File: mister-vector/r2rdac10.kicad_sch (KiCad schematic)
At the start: 20 parts

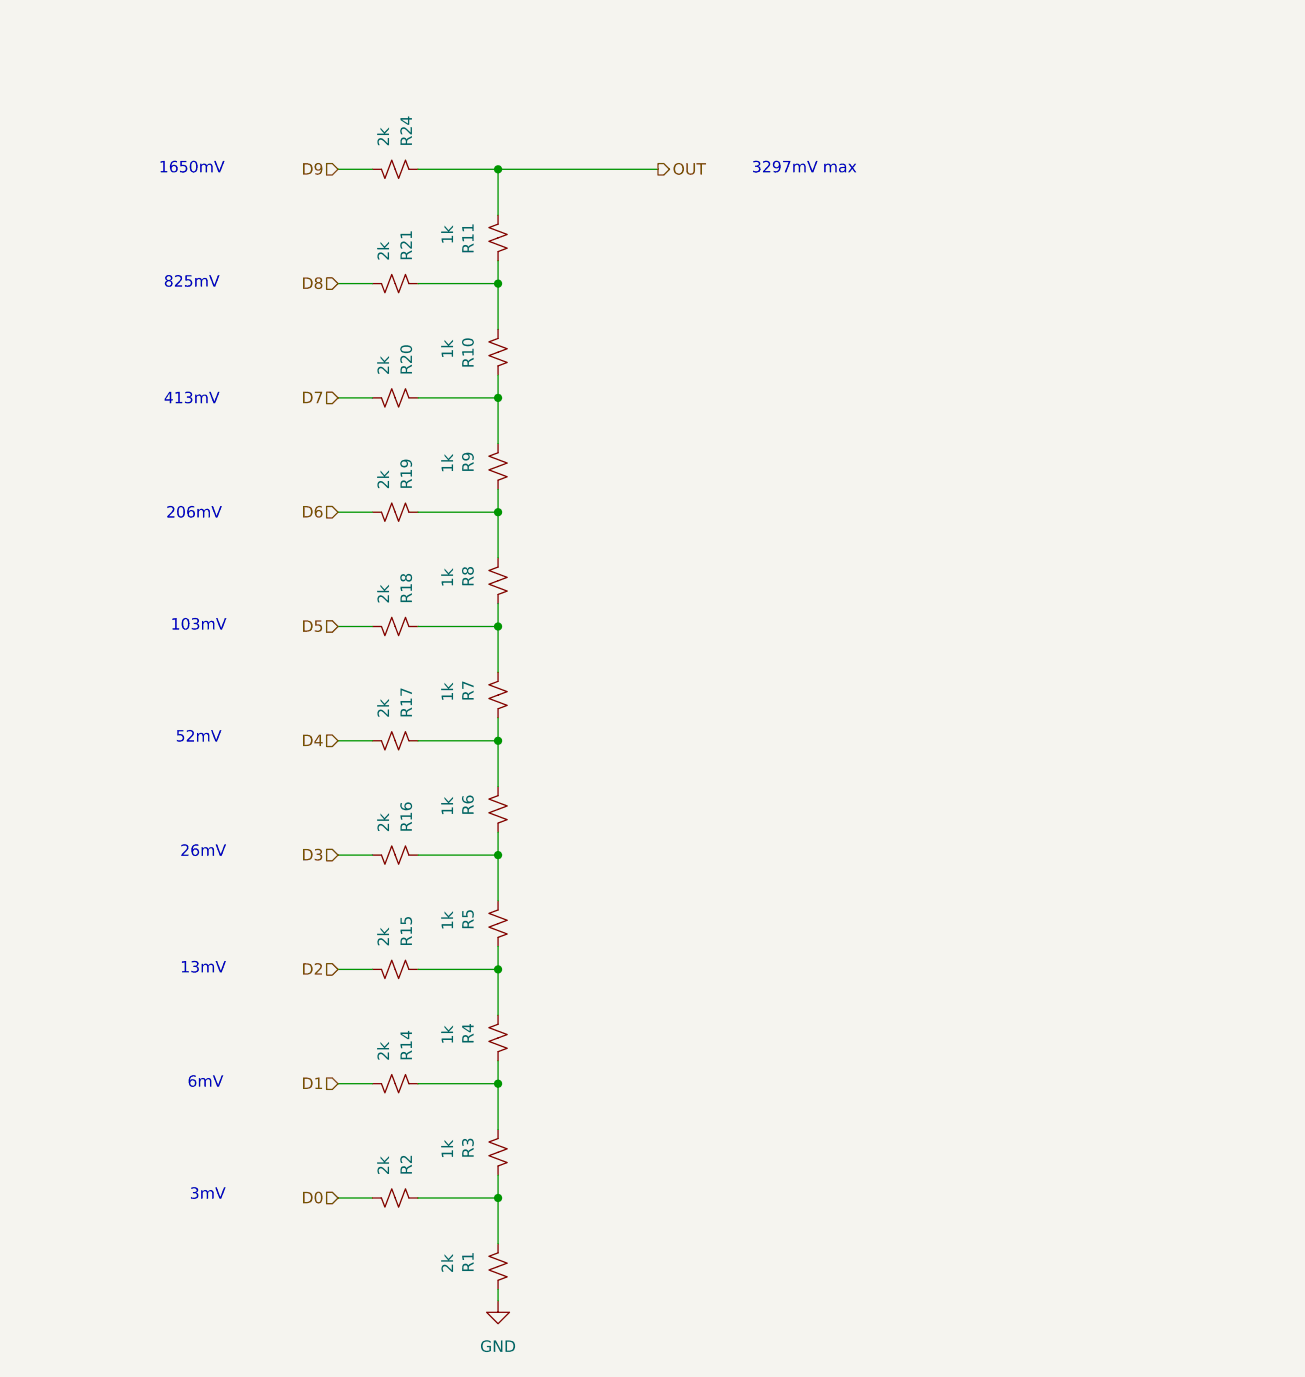
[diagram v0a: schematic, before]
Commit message: hierarchical schematic, add libraries
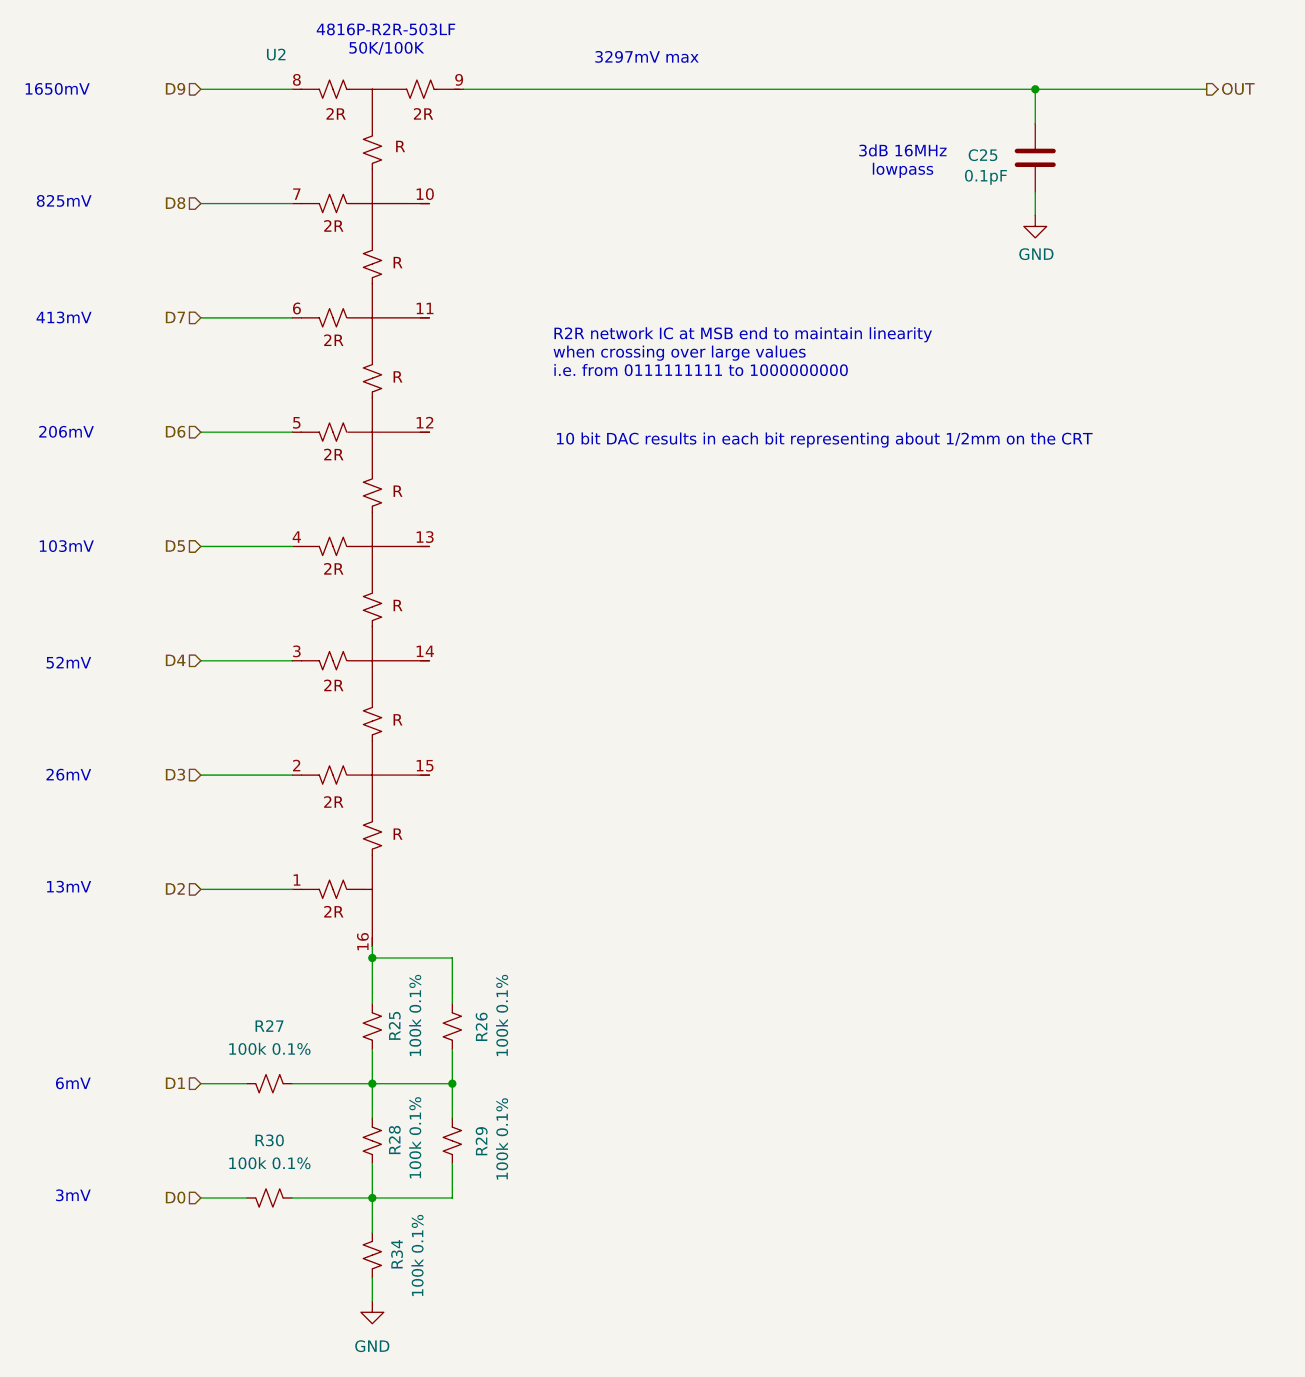
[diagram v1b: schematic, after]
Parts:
- removed R1, R14, R15, R16, R17, R18, R19, R2, R20, R21, R24: 2k, Resistor_SMD:R_0402_1005Metric, symbol Device:R_Small_US
- removed R10, R11, R3, R4, R5, R6, R7, R8, R9: 1k, Resistor_SMD:R_0402_1005Metric, symbol Device:R_Small_US
- added C25: 0.1pF, Capacitor_SMD:C_0402_1005Metric, symbol Device:C
- added R25, R26, R27, R28, R29, R30, R34: 100k 0.1%, Resistor_SMD:R_0402_1005Metric, symbol Device:R_Small_US
- added U2: 4816P-R2R-503LF, Package_SO:SOIC-16W_5.3x10.2mm_P1.27mm, symbol Device:4816P-R2R-503LF
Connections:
- net D0: now also R30.2
- net D1: now also R27.2
- net D2: now also U2.1
- net D3: now also U2.2
- net D4: now also U2.3
- net D5: now also U2.4
- net D6: now also U2.5
- net D7: now also U2.6
- net D8: now also U2.7
- net D9: now also U2.8
- net GND: now also C25.1, R34.2
- net OUT: now also C25.2, U2.9
- new net: R28.2, R29.2, R30.1, R34.1
- new net: R25.1, R26.1, U2.16
- new net: R25.2, R26.2, R27.1, R28.1, R29.1
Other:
- note added: "10 bit DAC results in each bit representing about 1/2mm on the CRT"
- note added: "3dB 16MHz lowpass"
- note added: "4816P-R2R-503LF 50K/100K"
- note added: "R2R network IC at MSB end to maintain linearity when crossing over large values i.e. from 0111111111 to 1000000000"
